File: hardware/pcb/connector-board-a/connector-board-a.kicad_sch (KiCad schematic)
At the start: 22 parts, among them J1 DE9_Pins, J2 8-215570-0, Q3 2N7002, U4 TPS63001

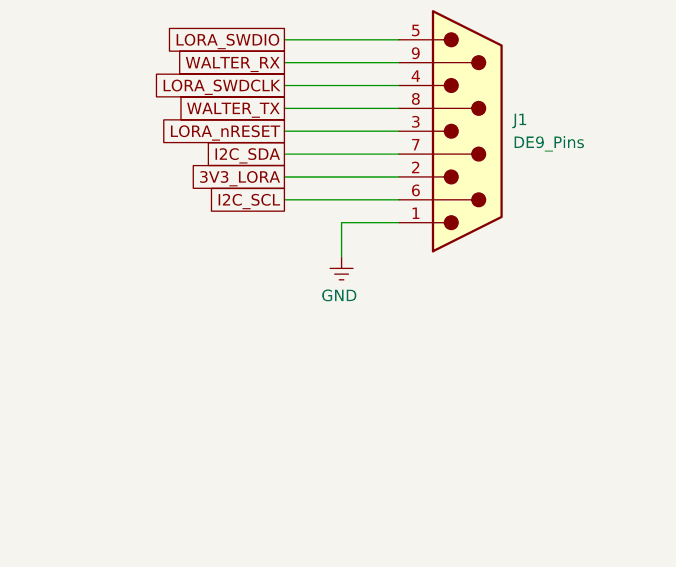
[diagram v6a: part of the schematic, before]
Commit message: Final PCB adjuments to rev 1.1
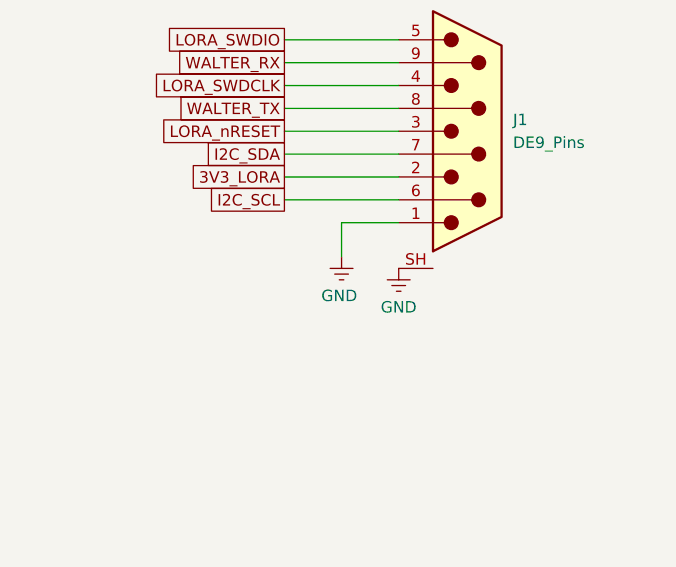
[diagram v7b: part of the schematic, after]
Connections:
- net GND: now also J1.SH
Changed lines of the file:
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@@
 		(pin "9"
+		)
+		(pin "SH"
 		)
 		(instances
@@
 					(unit 1)
 				)
+			)
+		)
+	)
+	(symbol
+		(lib_id "power:GND")
+		(at 203.2 52.07 0)
+		(unit 1)
+		(body_style 1)
+		(exclude_from_sim no)
+		(in_bom yes)
+		(on_board yes)
+		(in_pos_files yes)
+		(dnp no)
+		(property "Reference" "#PWR0203"
+			(at 205.232 50.8 0)
+			(hide yes)
+			(show_name no)
+			(do_not_autoplace no)
+			(effects
+				(font
+					(size 1.27 1.27)
+				)
+			)
+		)
+		(property "Value" "GND"
+			(at 203.2 56.388 0)
+			(show_name no)
+			(do_not_autoplace no)
+			(effects
+				(font
+					(size 1.27 1.27)
+				)
+			)
+		)
+		(property "Footprint" ""
+			(at 203.2 52.07 0)
+			(hide yes)
+			(show_name no)
+			(do_not_autoplace no)
+			(effects
+				(font
+					(size 1.27 1.27)
+				)
+			)
+		)
+		(property "Datasheet" ""
+			(at 203.2 52.07 0)
+			(hide yes)
+			(show_name no)
+			(do_not_autoplace no)
+			(effects
+				(font
+					(size 1.27 1.27)
+				)
+			)
+		)
+		(property "Description" ""
+			(at 203.2 52.07 0)
+			(show_name no)
+			(do_not_autoplace no)
+			(effects
+				(font
+					(size 1.27 1.27)
+				)
+			)
+		)
+		(pin "1"
+		)
+		(instances
+			(project "connector-board-a"
+				(path "/a5917824-ac3c-42e9-a83e-01bf9fc87273"
+					(reference "#PWR0203")
+					(unit 1)
+				)

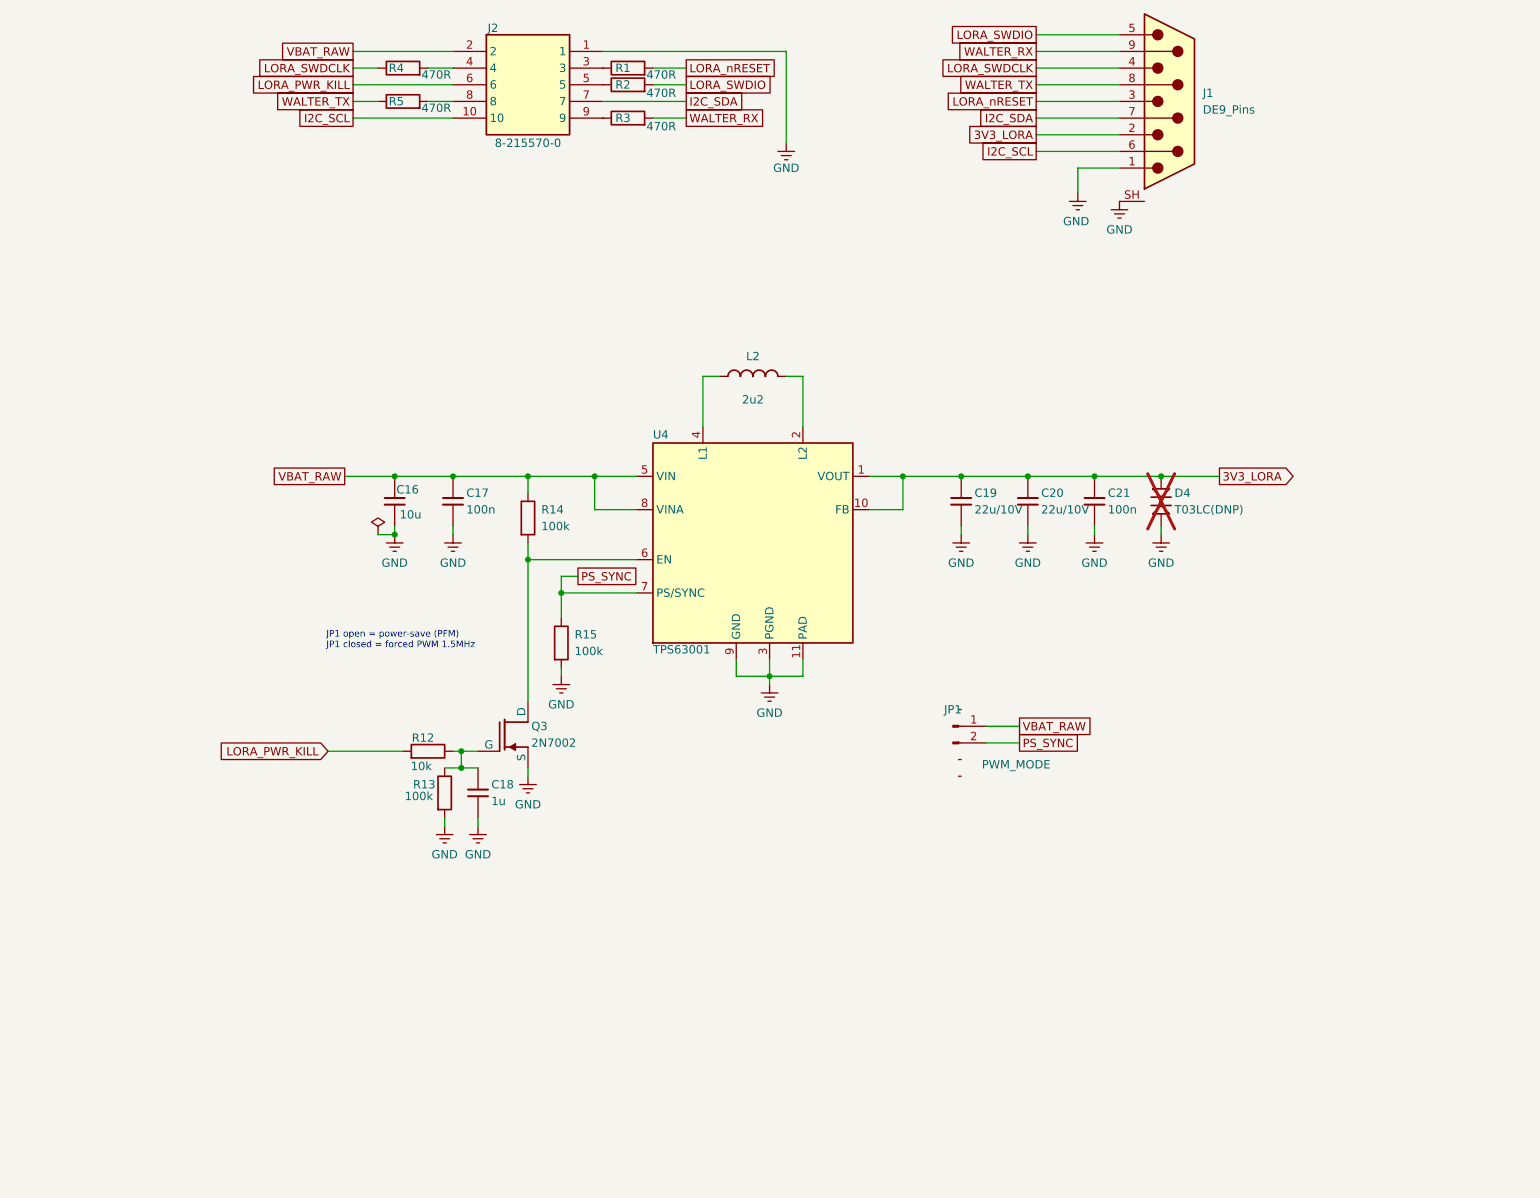
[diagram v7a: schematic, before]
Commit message: Added I2C environment sensor
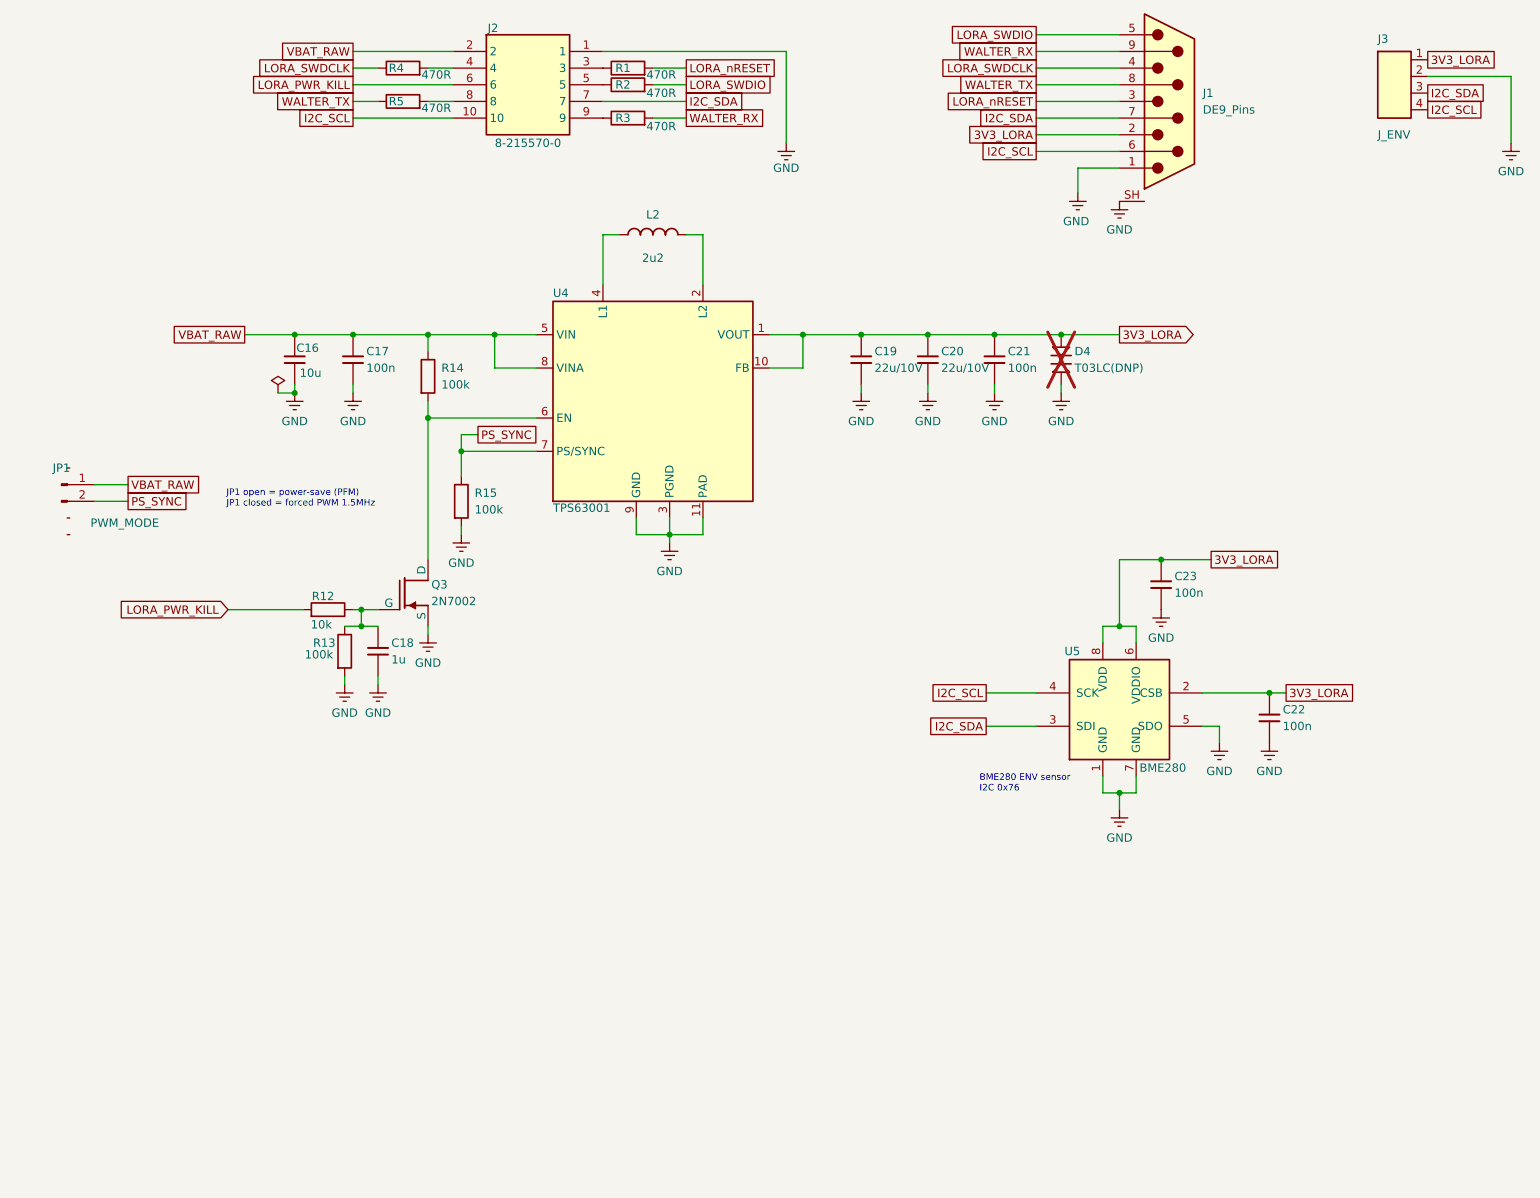
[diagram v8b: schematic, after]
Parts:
- added C22, C23: 100n, Capacitor_SMD:C_0603_1608Metric, symbol lora3v3:C_V
- added J3: J_ENV, Connector_PinHeader_2.54mm:PinHeader_1x04_P2.54mm_Vertical, symbol TwinOak:Conn_01x04
- added U5: BME280, Package_LGA:Bosch_LGA-8_2.5x2.5mm_P0.65mm_ClockwisePinNumbering, symbol TwinOak:BME280
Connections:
- net 3V3_LORA: now also C22.1, C23.1, J3.1 (Pin_1), U5.2 (CSB), U5.6 (VDDIO), U5.8 (VDD)
- net GND: now also C22.2, C23.2, J3.2 (Pin_2), U5.1 (GND), U5.5 (SDO), U5.7 (GND)
- net I2C_SCL: now also J3.4 (Pin_4), U5.4 (SCK)
- net I2C_SDA: now also J3.3 (Pin_3), U5.3 (SDI)
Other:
- note added: "BME280 ENV sensor I2C 0x76"
- moved on the sheet: C16, C17, C18, C19, C20, C21, D4, JP1, L2, Q3, R12, R13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
